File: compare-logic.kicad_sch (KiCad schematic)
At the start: 2 parts, among them U21002 4069

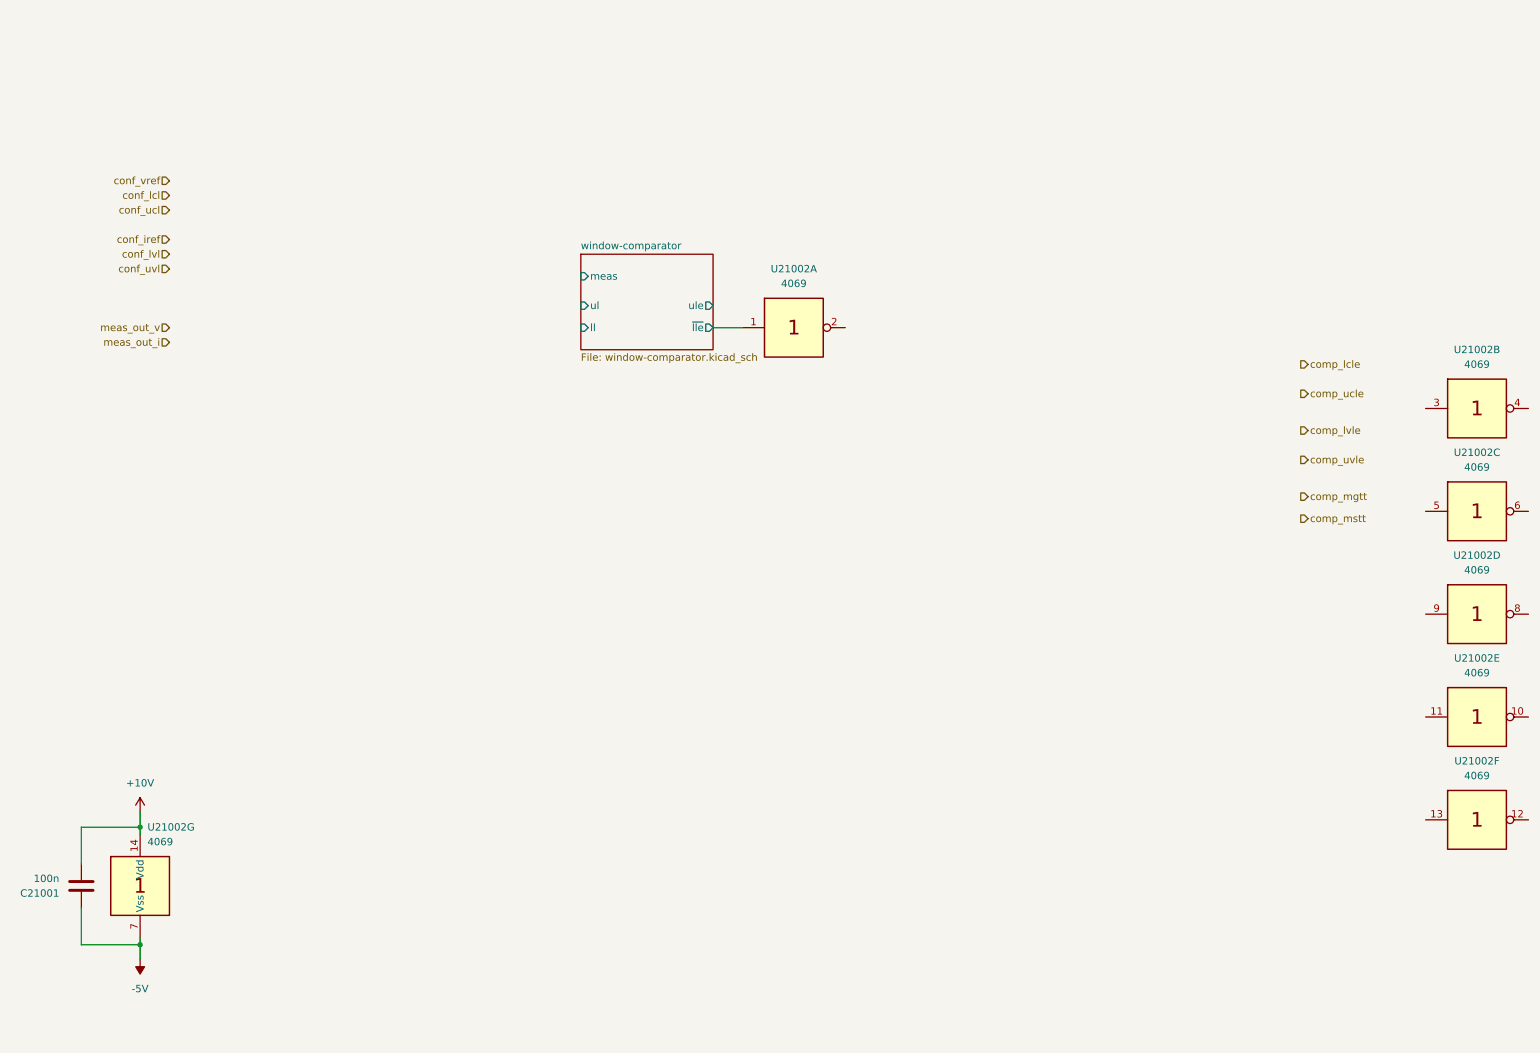
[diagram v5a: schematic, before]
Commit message: add window-comparator multiple instances for all configured limits and refs
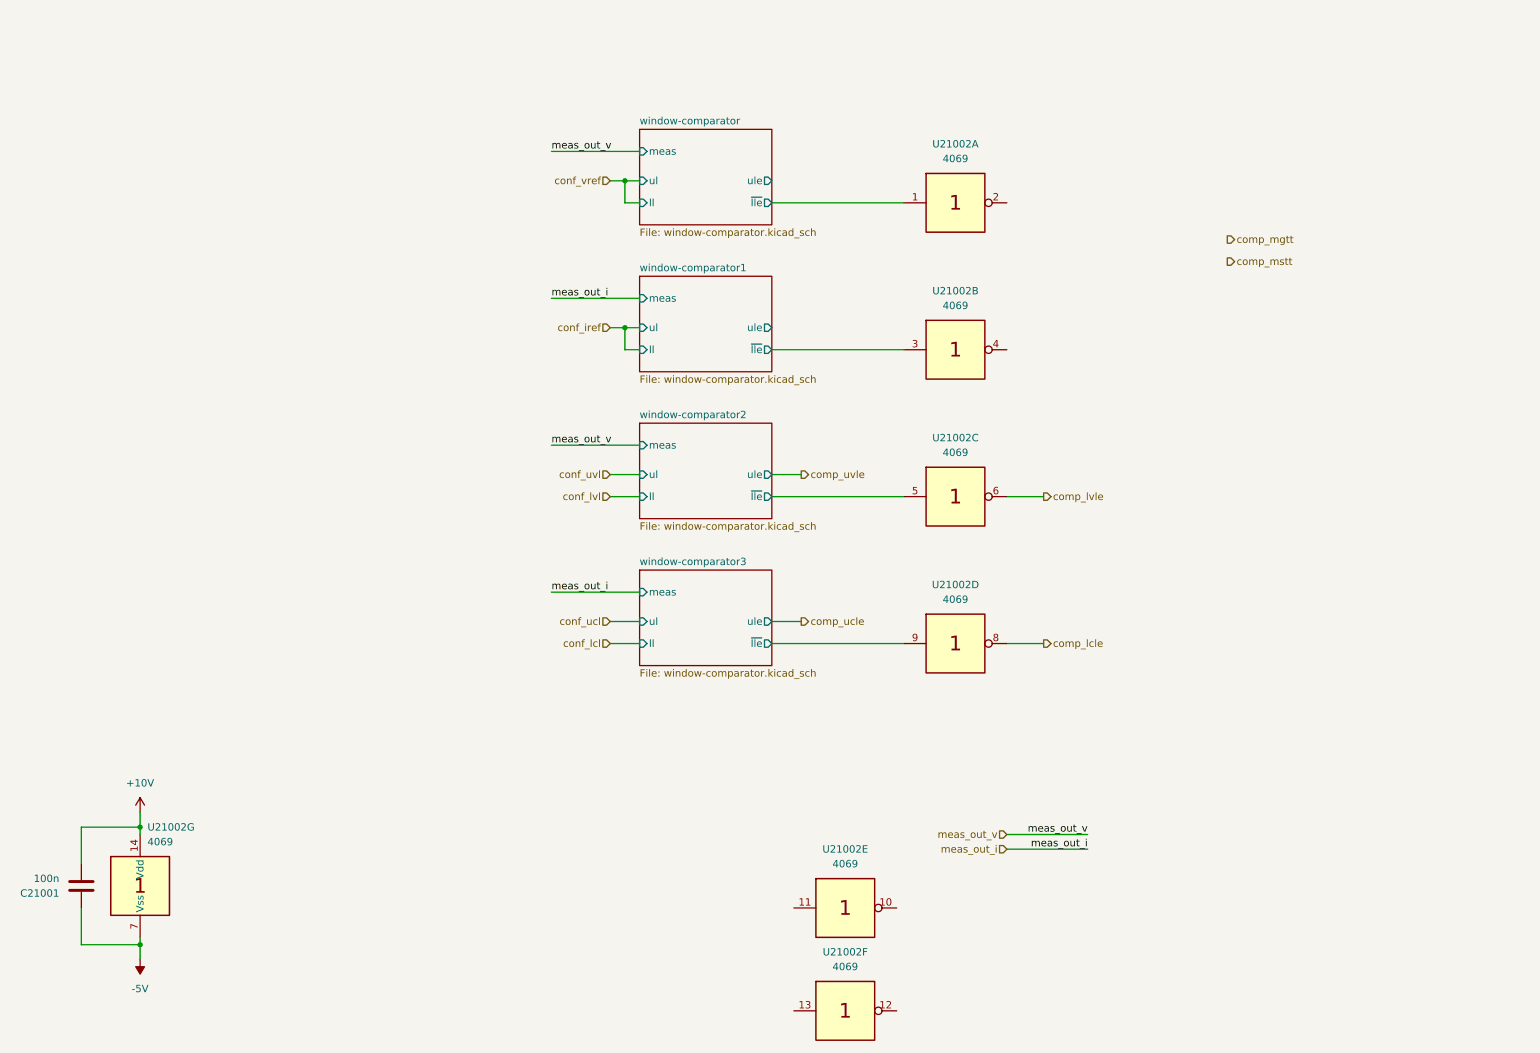
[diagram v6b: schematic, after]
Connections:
- net comp_lcle: now also U21002.8
- net comp_lvle: now also U21002.6
- net window-comparator1/~{lle}: now reaches U21002.3
- net window-comparator2/~{lle}: now reaches U21002.5
- net window-comparator3/~{lle}: now reaches U21002.9
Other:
- added sheet window-comparator1 (window-comparator.kicad_sch)
- added sheet window-comparator2 (window-comparator.kicad_sch)
- added sheet window-comparator3 (window-comparator.kicad_sch)
- moved on the sheet: U21002A, U21002B, U21002C, U21002D, U21002E, U21002F

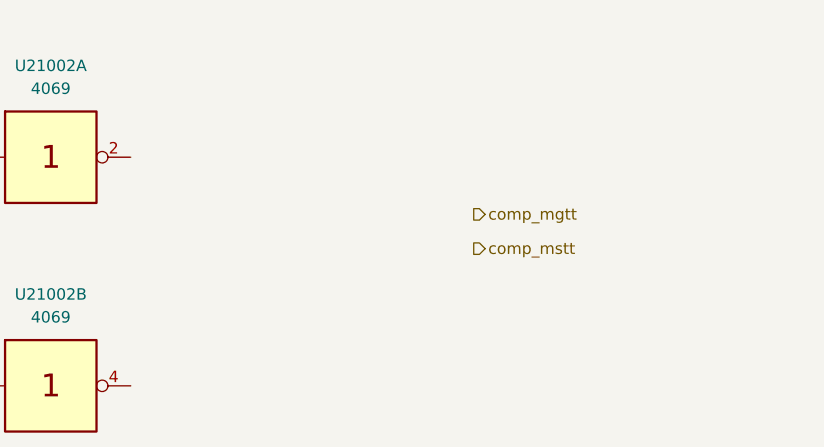
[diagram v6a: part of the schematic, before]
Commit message: add compare-logic conf_refselect hirarchical input
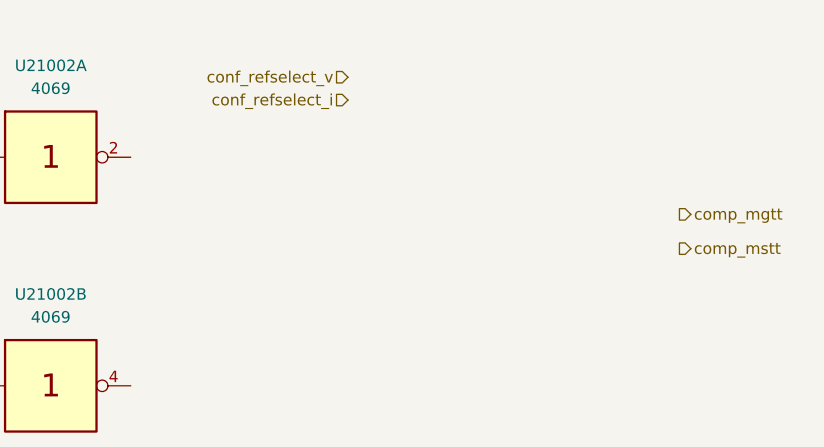
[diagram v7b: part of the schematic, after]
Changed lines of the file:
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@@
+		)
+	)
+	(hierarchical_label "conf_refselect_i"
+		(shape input)
+		(at 214.63 44.45 180)
+		(fields_autoplaced yes)
+		(effects
+			(font
+				(size 1.27 1.27)
+			)
+			(justify right)
 		)
 	)
@@
 		)
 	)
+	(hierarchical_label "conf_refselect_v"
+		(shape input)
+		(at 214.63 41.91 180)
+		(fields_autoplaced yes)
+		(effects
+			(font
+				(size 1.27 1.27)
+			)
+			(justify right)
+		)
+	)
 	(hierarchical_label "comp_mstt"
 		(shape output)
-		(at 228.6 60.96 0)
+		(at 251.46 60.96 0)
 		(fields_autoplaced yes)
 		(effects
@@
 	(hierarchical_label "comp_mgtt"
 		(shape output)
-		(at 228.6 57.15 0)
+		(at 251.46 57.15 0)
 		(fields_autoplaced yes)
 		(effects

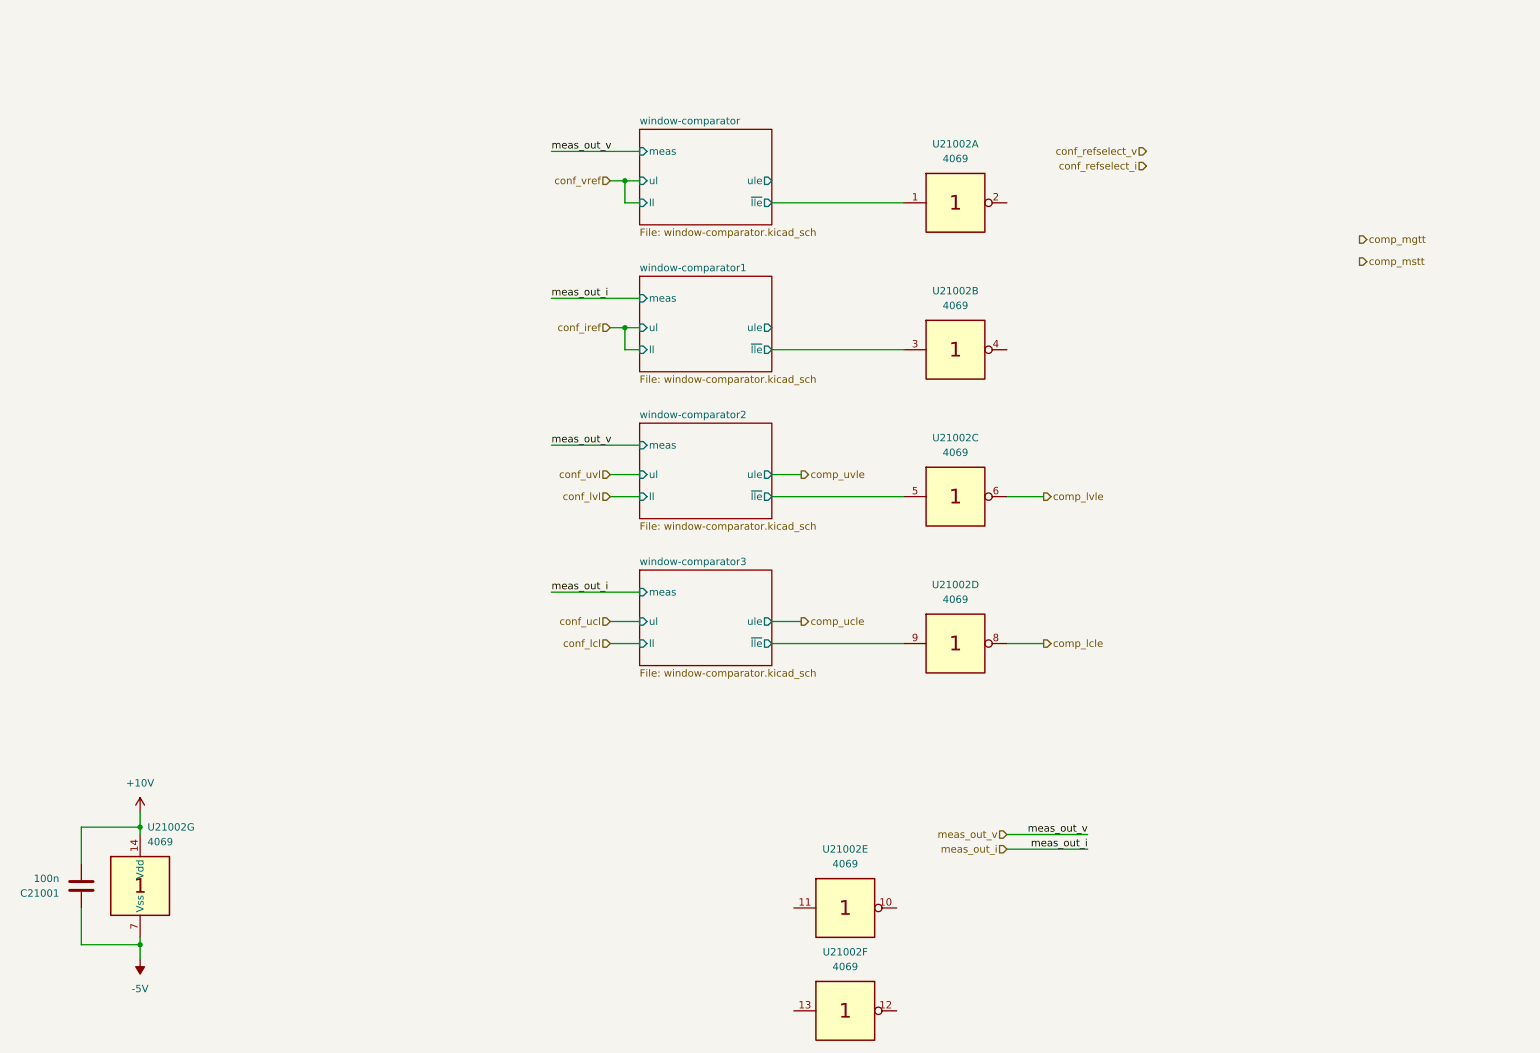
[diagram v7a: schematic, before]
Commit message: add compare-logic 4019 select gate
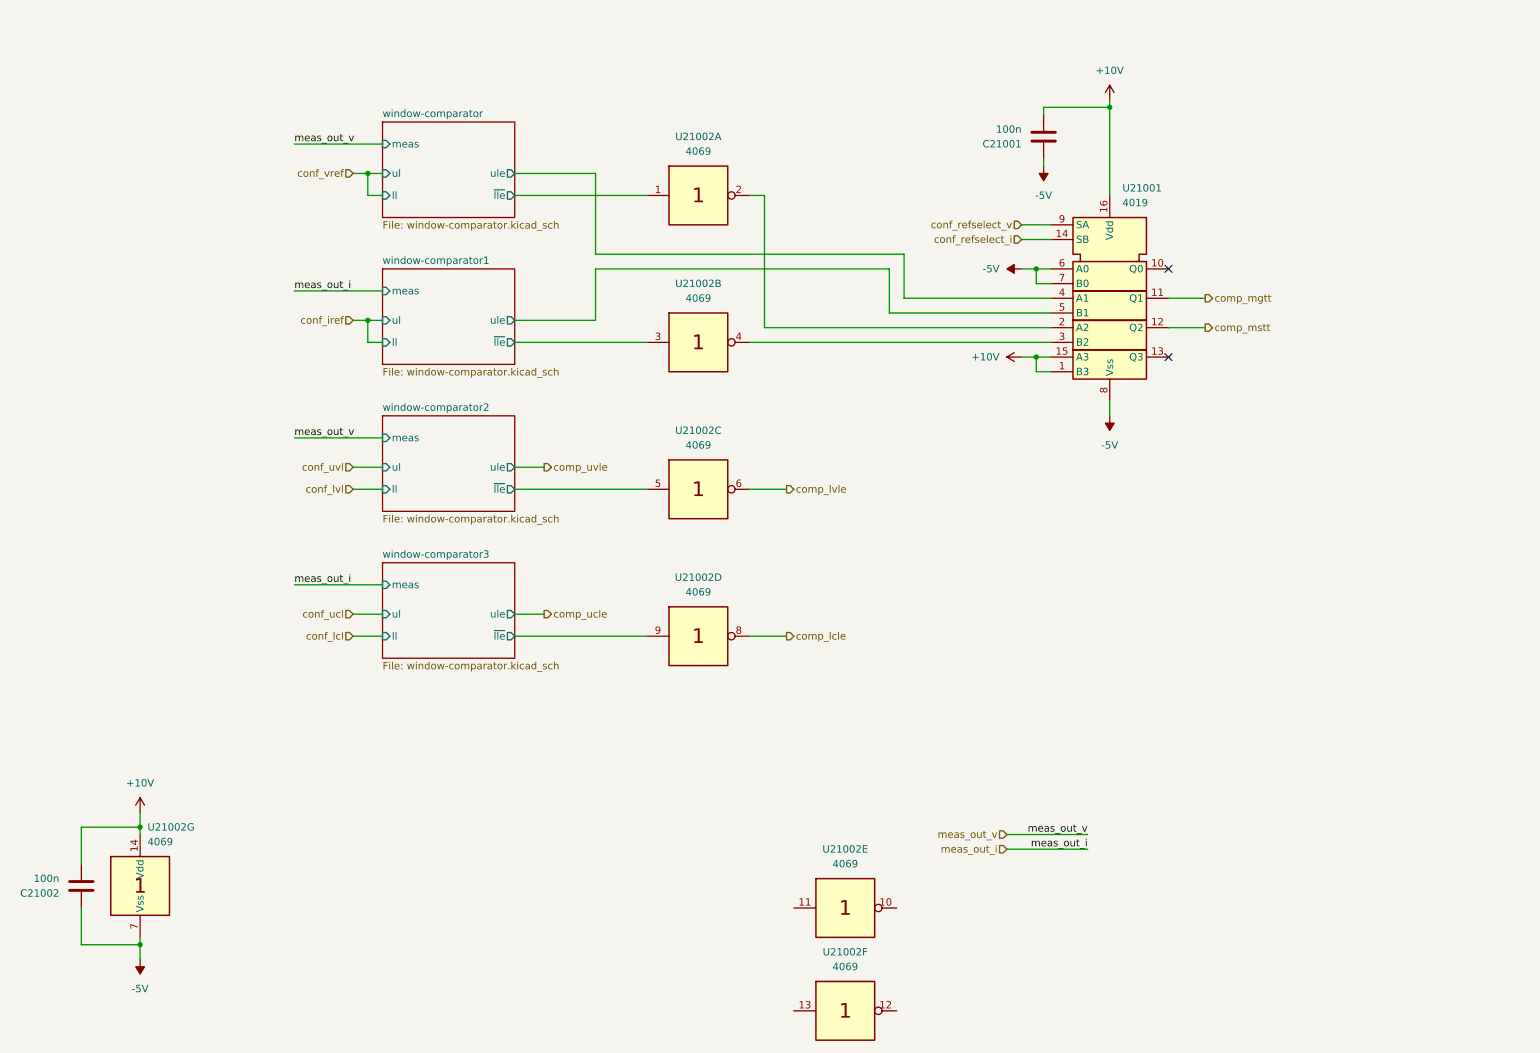
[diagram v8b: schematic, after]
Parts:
- added C21002: 100n, Capacitor_SMD:C_0805_2012Metric_Pad1.18x1.45mm_HandSolder, symbol pss:C
- added U21001: 4019, Package_SO:SOIC-16_3.9x9.9mm_P1.27mm, symbol pss:4019
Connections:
- net +10V: now also C21002.2, U21001.1 (B3), U21001.15 (A3), U21001.16 (Vdd)
- net -5V: now also C21002.1, U21001.6 (A0), U21001.7 (B0), U21001.8 (Vss)
- net comp_mgtt: now also U21001.11 (Q1)
- net comp_mstt: now also U21001.12 (Q2)
- net conf_refselect_i: now also U21001.14 (SB)
- net conf_refselect_v: now also U21001.9 (SA)
- net window-comparator/ule: now also U21001.4 (A1)
- net window-comparator1/ule: now also U21001.5 (B1)
- net at U21002.4: now also U21001.3 (B2)
- net at U21002.2: now also U21001.2 (A2)
- no-connect marks 0 -> 2
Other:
- moved on the sheet: C21001, U21002A, U21002B, U21002C, U21002D
